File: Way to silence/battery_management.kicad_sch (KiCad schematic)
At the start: 21 parts

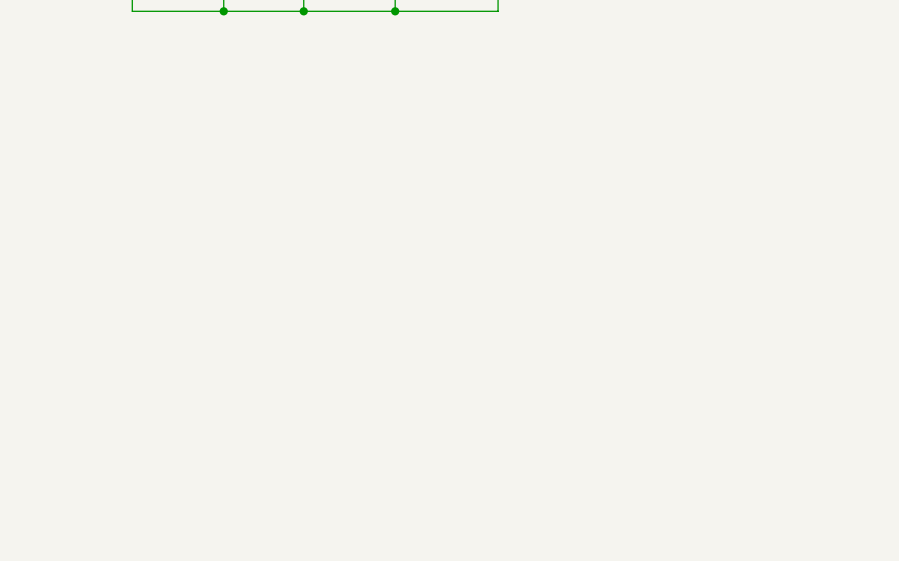
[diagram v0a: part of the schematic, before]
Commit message: [ADD] Retro-engineering BMS notes
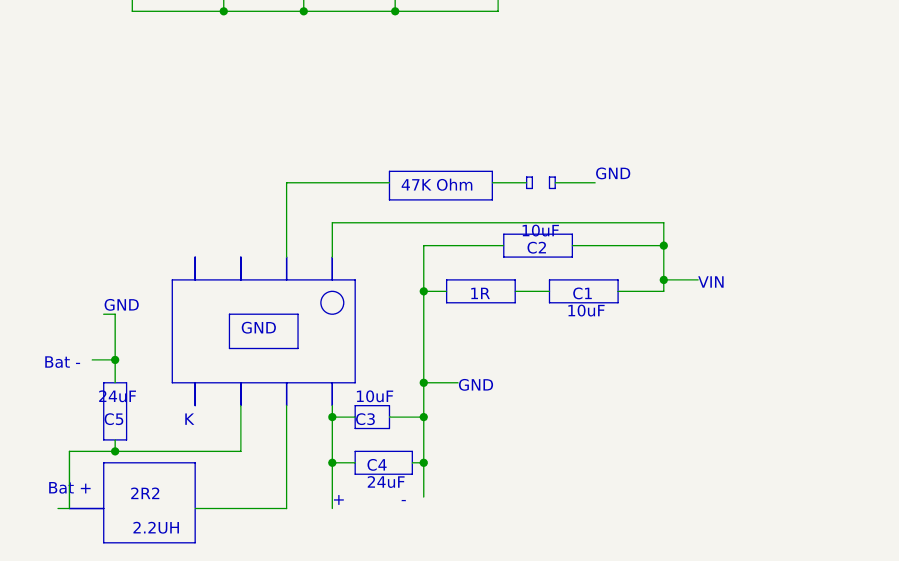
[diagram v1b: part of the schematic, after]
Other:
- note added: "+"
- note added: "-"
- note added: "10uF"
- note added: "1R"
- note added: "2.2UH"
- note added: "24uF"
- note added: "2R2"
- note added: "47K Ohm"
- note added: "Bat +"
- note added: "Bat -"
- note added: "C1"
- note added: "C2"
- note added: "C3"
- note added: "C4"
- note added: "C5"
- note added: "GND"
- note added: "K"
- note added: "VIN"

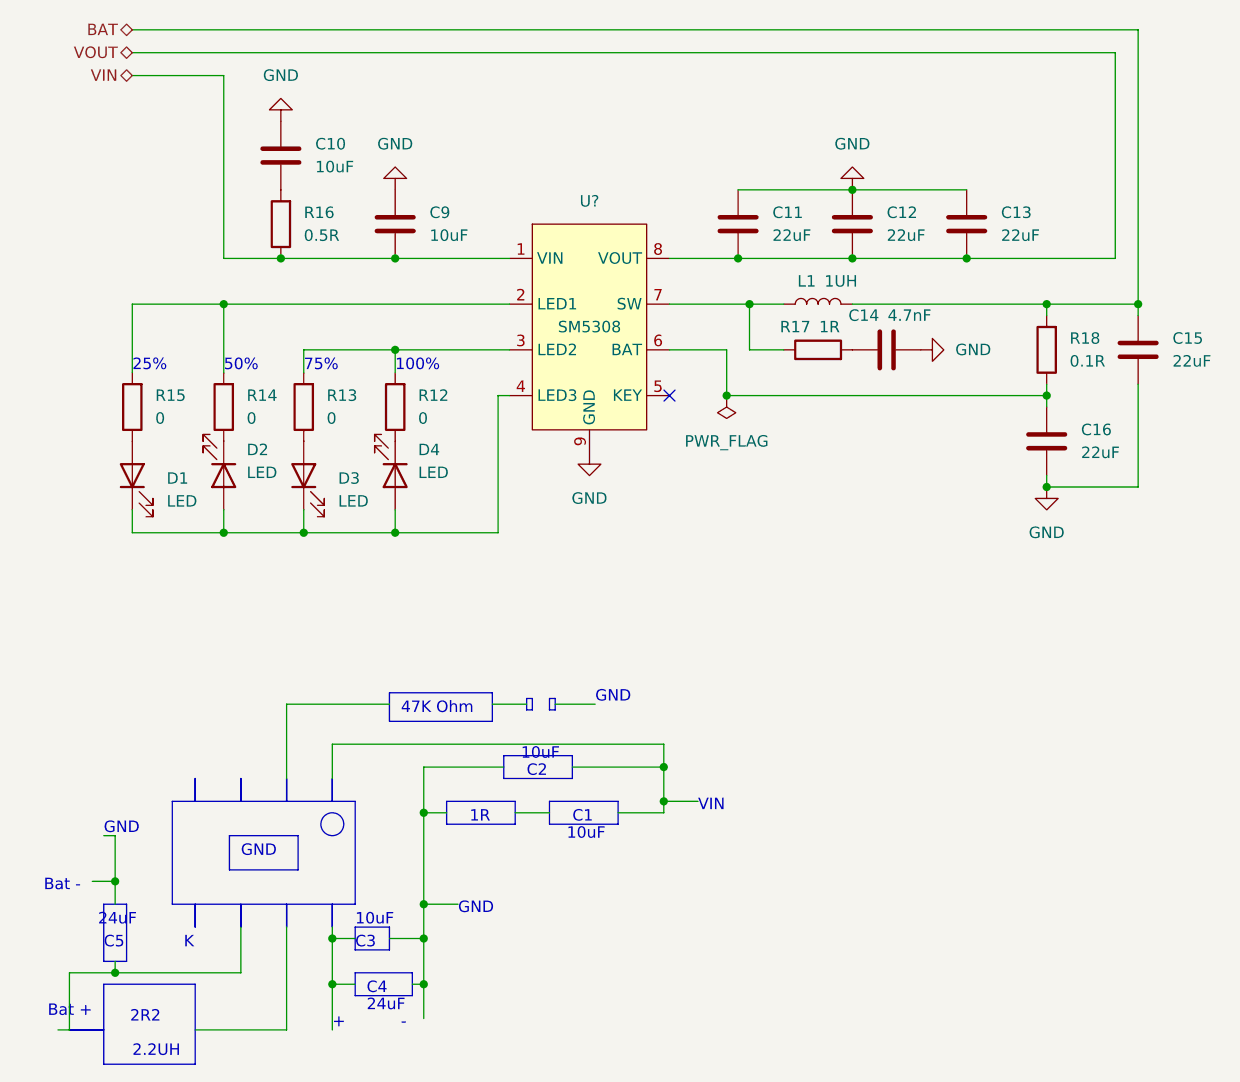
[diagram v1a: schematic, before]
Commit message: [UDPT] Schematics from retro-engineering
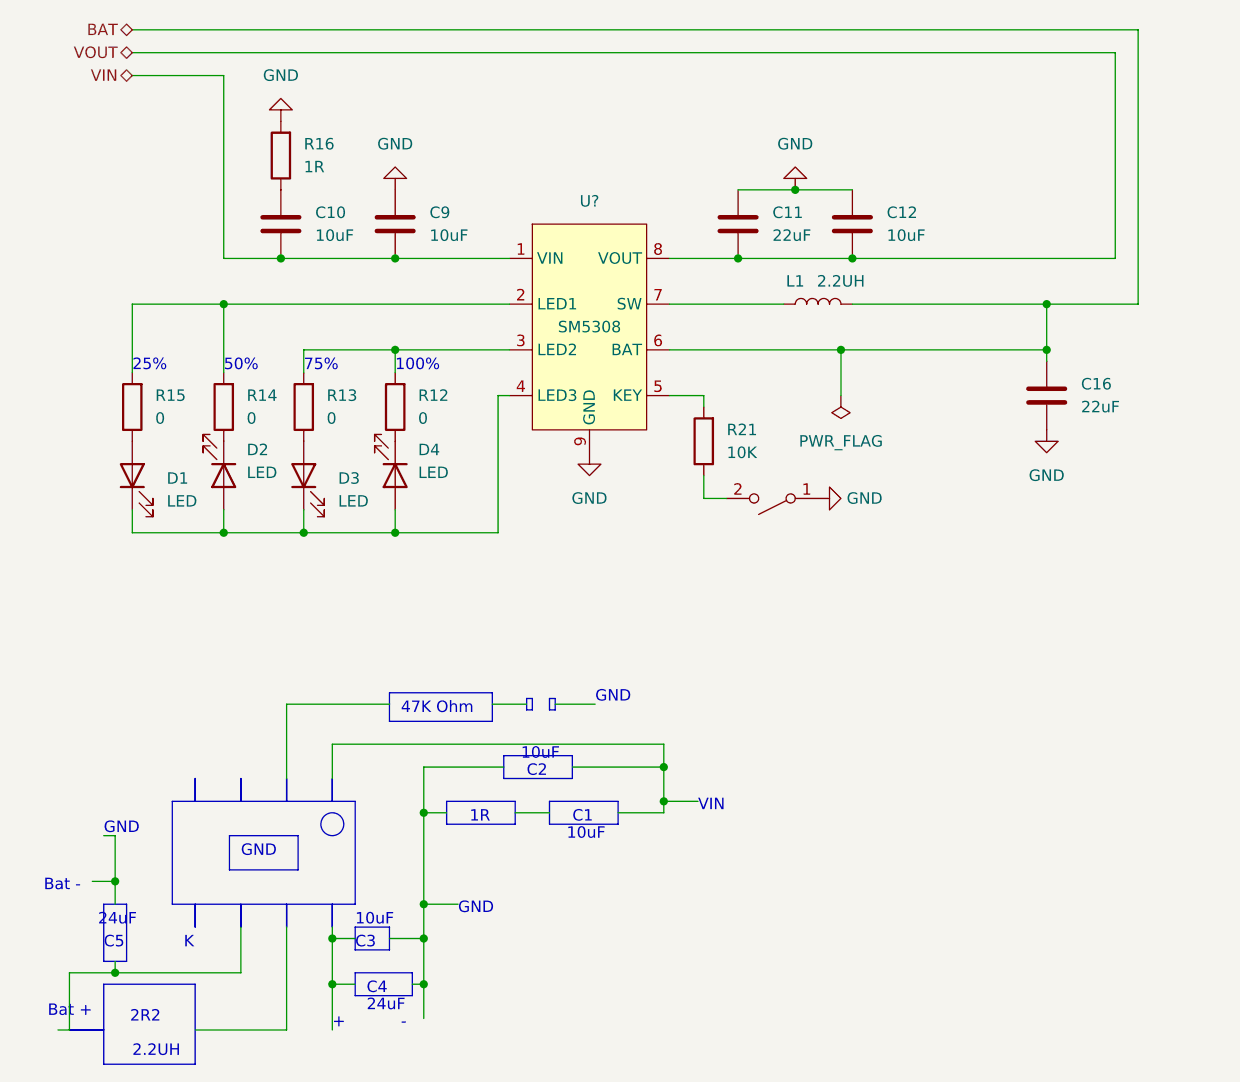
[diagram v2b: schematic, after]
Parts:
- removed C13, C15: 22uF, Way to silence:C_0603_1608Metric, symbol Way to silence:C
- removed C14: 4.7nF, Way to silence:C_0603_1608Metric, symbol Way to silence:C
- removed R17: 1R, Way to silence:R_0603_1608Metric, symbol Way to silence:R
- removed R18: 0.1R, Way to silence:R_0603_1608Metric, symbol Way to silence:R
- added R21: 10K, Way to silence:R_0603_1608Metric, symbol Way to silence:R
- added SW3: SW_SPST, Way to silence:SW_SPST, symbol Way to silence:SW_SPST
- C12: value 22uF -> 10uF; LCSC C59461 -> C77041
- L1: value 1UH -> 2.2UH; LCSC C2847468 -> C5189746
- R16: value 0.5R -> 1R; LCSC C2934253 -> C25212
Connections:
- net BAT: now also C16.2, U?.6 (BAT)
- net GND: now also R16.2, SW3.1 (A); no longer C10.2
- net VIN: now also C10.1; no longer R16.1
- net at U?.5 (KEY): now also R21.2
- new net: C10.2, R16.1
- new net: R21.1, SW3.2 (B)
- no-connect marks 1 -> 0
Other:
- moved on the sheet: C10, C16, R16

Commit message: [UDPT] Pcb from schematics
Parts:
- L1: footprint Way to silence:Inductor -> Way to silence:Inductor-0630LR
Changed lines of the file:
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@@
       (effects (font (size 1.27 1.27)))
     )
-    (property "Footprint" "Way to silence:Inductor" (at 101.6 48.26 90)
+    (property "Footprint" "Way to silence:Inductor-0630LR" (at 101.6 48.26 90)
       (effects (font (size 1.27 1.27)) hide)
     )

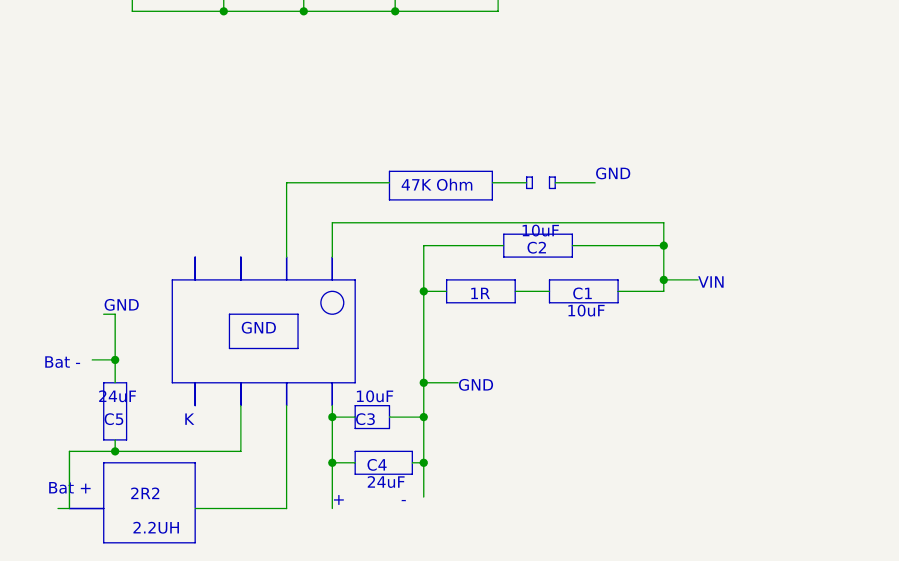
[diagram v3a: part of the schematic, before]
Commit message: [CLEAN] Remove retro-engineering drawing
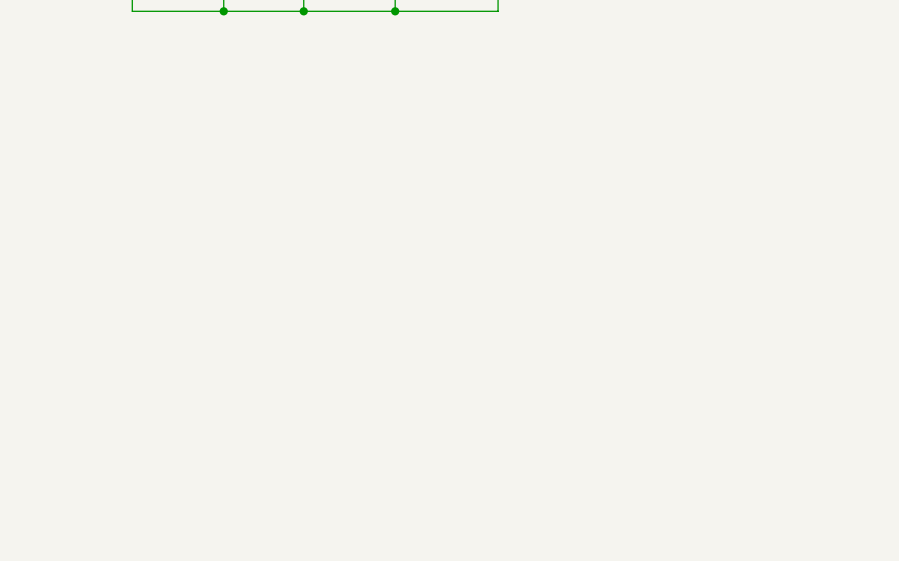
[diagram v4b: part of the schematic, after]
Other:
- note removed: "+"
- note removed: "-"
- note removed: "10uF"
- note removed: "1R"
- note removed: "2.2UH"
- note removed: "24uF"
- note removed: "2R2"
- note removed: "47K Ohm"
- note removed: "Bat +"
- note removed: "Bat -"
- note removed: "C1"
- note removed: "C2"
- note removed: "C3"
- note removed: "C4"
- note removed: "C5"
- note removed: "GND"
- note removed: "K"
- note removed: "VIN"
